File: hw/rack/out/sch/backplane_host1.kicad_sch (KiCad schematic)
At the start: 17 parts, among them J2 CM4IO J8, U4 SC16IS752IPW, U5 SC16IS752IPW, Y1 14.7456M, Y2 14.7456M

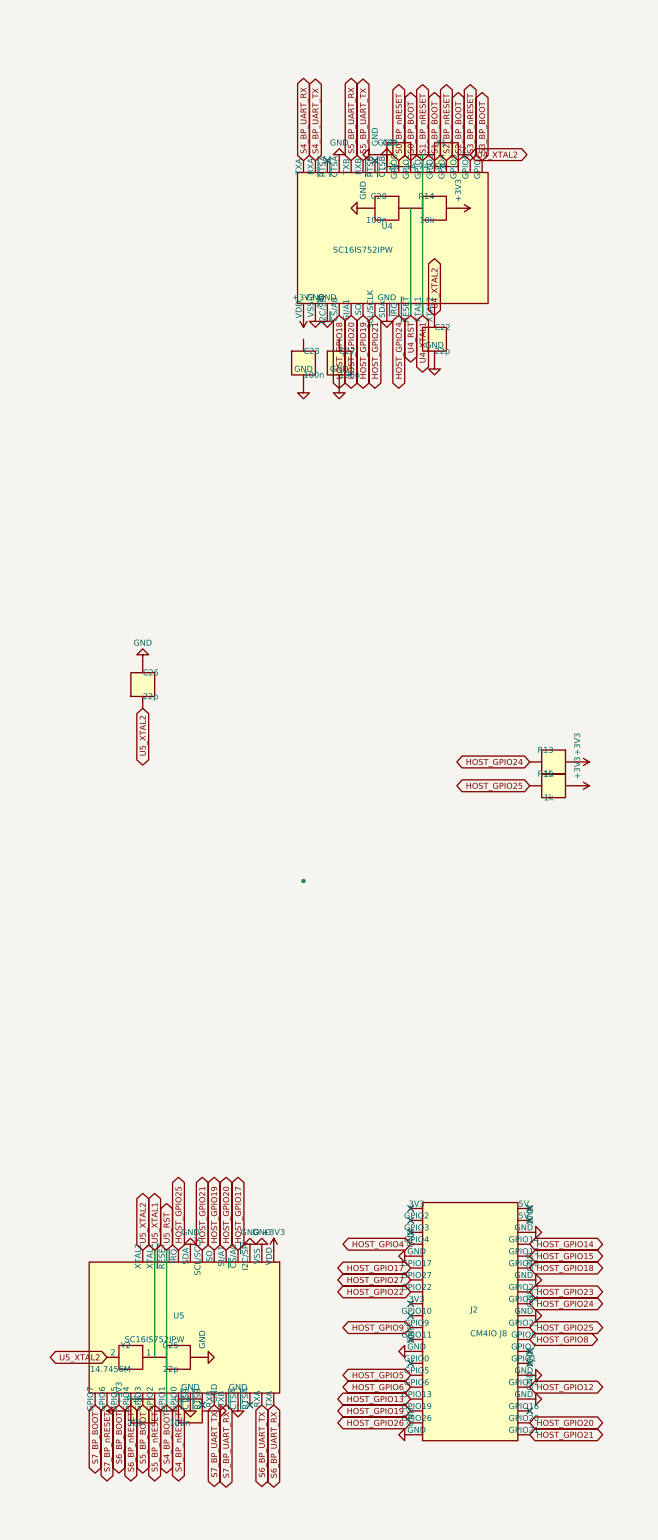
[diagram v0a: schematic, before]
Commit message: hw/rack: #95 review fixes: QPQ1907 pinout + RF continuity test, 1 ohm 2512 bias-T, input fuse, keyed slots, CM4 source, CI scikit-rf + stale check, ADR-0018 gain-plan stop-and-ask (#33)
- QPQ1907 pins per datasheet 040820 (1 in, 4 out, 2/3/5 GND); test walks BNC to every slot port
- bias-T 1 ohm 2512 (0.27 W at 0.52 A), resistor power ratings asserted
- 4 A fuse ahead of the TVS; Harwin M20-7831346 + M20-003 key at position 14
- CM4002008 from The Pi Hut (GBP 79.20); Lite-On LEDs
- Wilkinson +-10 % width sweep; netlist timestamp stripped
- CI: scikit-rf installed, cross-check required under CI, hw/rack stale-output diff
- Audit 6: per-carrier NF, stage headroom at 0.5/1/1.5 m (wings), phones, nRF5340 PS v1.1
  C/I + PIMD, nRF21540 P1dB; no fixed gain plan meets both: stop-and-ask

Co-Authored-By: Claude Opus 5.5 <noreply@anthropic.com>
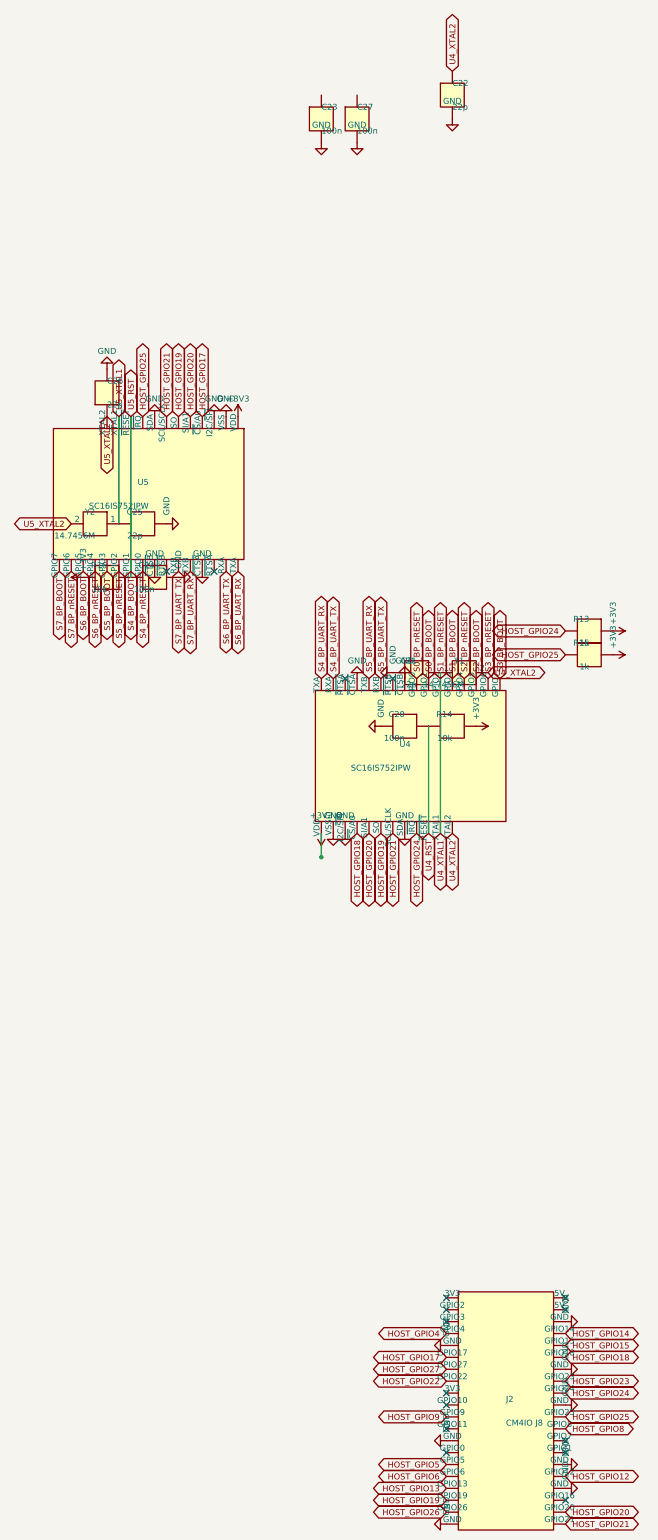
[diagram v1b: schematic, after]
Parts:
- R13, R14, R15, R16: P_W (none) -> 0.0625
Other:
- moved on the sheet: C20, C21, C22, C23, C24, C25, C26, C27, J2, R13, R14, R15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
